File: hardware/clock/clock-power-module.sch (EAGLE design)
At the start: 13 parts, among them U3 L7805, U5 LTC6900IS5PBF

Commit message: main board starting to route
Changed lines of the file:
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@@
 <grid distance="0.1" unitdist="inch" unit="inch" style="lines" multiple="1" display="no" altdistance="0.01" altunitdist="inch" altunit="inch"/>
 <layers>
-<layer number="1" name="Top" color="4" fill="1" visible="yes" active="no"/>
-<layer number="2" name="Route2" color="16" fill="1" visible="yes" active="no"/>
-<layer number="3" name="Route3" color="17" fill="1" visible="yes" active="no"/>
-<layer number="4" name="Route4" color="18" fill="1" visible="yes" active="no"/>
-<layer number="5" name="Route5" color="19" fill="1" visible="yes" active="no"/>
-<layer number="6" name="Route6" color="25" fill="1" visible="yes" active="no"/>
-<layer number="7" name="Route7" color="26" fill="1" visible="yes" active="no"/>
-<layer number="8" name="Route8" color="27" fill="1" visible="yes" active="no"/>
-<layer number="9" name="Route9" color="28" fill="1" visible="yes" active="no"/>
-<layer number="10" name="Route10" color="29" fill="1" visible="yes" active="no"/>
-<layer number="11" name="Route11" color="30" fill="1" visible="yes" active="no"/>
-<layer number="12" name="Route12" color="20" fill="1" visible="yes" active="no"/>
-<layer number="13" name="Route13" color="21" fill="1" visible="yes" active="no"/>
-<layer number="14" name="Route14" color="22" fill="1" visible="yes" active="no"/>
-<layer number="15" name="Route15" color="23" fill="1" visible="yes" active="no"/>
-<layer number="16" name="Bottom" color="1" fill="1" visible="yes" active="no"/>
-<layer number="17" name="Pads" color="2" fill="1" visible="yes" active="no"/>
-<layer number="18" name="Vias" color="2" fill="1" visible="yes" active="no"/>
-<layer number="19" name="Unrouted" color="6" fill="1" visible="yes" active="no"/>
-<layer number="20" name="Dimension" color="24" fill="1" visible="yes" active="no"/>
-<layer number="21" name="tPlace" color="7" fill="1" visible="yes" active="no"/>
-<layer number="22" name="bPlace" color="7" fill="1" visible="yes" active="no"/>
-<layer number="23" name="tOrigins" color="15" fill="1" visible="yes" active="no"/>
-<layer number="24" name="bOrigins" color="15" fill="1" visible="yes" active="no"/>
-<layer number="25" name="tNames" color="7" fill="1" visible="yes" active="no"/>
-<layer number="26" name="bNames" color="7" fill="1" visible="yes" active="no"/>
-<layer number="27" name="tValues" color="7" fill="1" visible="yes" active="no"/>
-<layer number="28" name="bValues" color="7" fill="1" visible="yes" active="no"/>
+<layer number="1" name="Top" color="4" fill="1" visible="no" active="no"/>
+<layer number="2" name="Route2" color="16" fill="1" visible="no" active="no"/>
+<layer number="3" name="Route3" color="17" fill="1" visible="no" active="no"/>
+<layer number="4" name="Route4" color="18" fill="1" visible="no" active="no"/>
+<layer number="5" name="Route5" color="19" fill="1" visible="no" active="no"/>
+<layer number="6" name="Route6" color="25" fill="1" visible="no" active="no"/>
+<layer number="7" name="Route7" color="26" fill="1" visible="no" active="no"/>
+<layer number="8" name="Route8" color="27" fill="1" visible="no" active="no"/>
+<layer number="9" name="Route9" color="28" fill="1" visible="no" active="no"/>
+<layer number="10" name="Route10" color="29" fill="1" visible="no" active="no"/>
+<layer number="11" name="Route11" color="30" fill="1" visible="no" active="no"/>
+<layer number="12" name="Route12" color="20" fill="1" visible="no" active="no"/>
+<layer number="13" name="Route13" color="21" fill="1" visible="no" active="no"/>
+<layer number="14" name="Route14" color="22" fill="1" visible="no" active="no"/>
+<layer number="15" name="Route15" color="23" fill="1" visible="no" active="no"/>
+<layer number="16" name="Bottom" color="1" fill="1" visible="no" active="no"/>
+<layer number="17" name="Pads" color="2" fill="1" visible="no" active="no"/>
+<layer number="18" name="Vias" color="2" fill="1" visible="no" active="no"/>
+<layer number="19" name="Unrouted" color="6" fill="1" visible="no" active="no"/>
+<layer number="20" name="Dimension" color="24" fill="1" visible="no" active="no"/>
+<layer number="21" name="tPlace" color="7" fill="1" visible="no" active="no"/>
+<layer number="22" name="bPlace" color="7" fill="1" visible="no" active="no"/>
+<layer number="23" name="tOrigins" color="15" fill="1" visible="no" active="no"/>
+<layer number="24" name="bOrigins" color="15" fill="1" visible="no" active="no"/>
+<layer number="25" name="tNames" color="7" fill="1" visible="no" active="no"/>
+<layer number="26" name="bNames" color="7" fill="1" visible="no" active="no"/>
+<layer number="27" name="tValues" color="7" fill="1" visible="no" active="no"/>
+<layer number="28" name="bValues" color="7" fill="1" visible="no" active="no"/>
 <layer number="29" name="tStop" color="7" fill="3" visible="no" active="no"/>
 <layer number="30" name="bStop" color="7" fill="6" visible="no" active="no"/>
@@
 <layer number="35" name="tGlue" color="7" fill="4" visible="no" active="no"/>
 <layer number="36" name="bGlue" color="7" fill="5" visible="no" active="no"/>
-<layer number="37" name="tTest" color="7" fill="1" visible="yes" active="no"/>
-<layer number="38" name="bTest" color="7" fill="1" visible="yes" active="no"/>
+<layer number="37" name="tTest" color="7" fill="1" visible="no" active="no"/>
+<layer number="38" name="bTest" color="7" fill="1" visible="no" active="no"/>
 <layer number="39" name="tKeepout" color="4" fill="11" visible="no" active="no"/>
 <layer number="40" name="bKeepout" color="1" fill="11" visible="no" active="no"/>
@@
 <layer number="44" name="Drills" color="7" fill="1" visible="no" active="no"/>
 <layer number="45" name="Holes" color="7" fill="1" visible="no" active="no"/>
-<layer number="46" name="Milling" color="3" fill="1" visible="yes" active="no"/>
-<layer number="47" name="Measures" color="7" fill="1" visible="yes" active="no"/>
-<layer number="48" name="Document" color="7" fill="1" visible="yes" active="no"/>
-<layer number="49" name="Reference" color="7" fill="1" visible="yes" active="no"/>
-<layer number="50" name="dxf" color="7" fill="1" visible="yes" active="no"/>
-<layer number="51" name="tDocu" color="7" fill="1" visible="yes" active="no"/>
-<layer number="52" name="bDocu" color="7" fill="1" visible="yes" active="no"/>
-<layer number="53" name="tGND_GNDA" color="7" fill="9" visible="yes" active="no"/>
-<layer number="54" name="bGND_GNDA" color="1" fill="9" visible="yes" active="no"/>
-<layer number="56" name="wert" color="7" fill="1" visible="yes" active="no"/>
-<layer number="57" name="tCAD" color="7" fill="1" visible="yes" active="no"/>
-<layer number="59" name="tCarbon" color="7" fill="1" visible="yes" active="no"/>
-<layer number="60" name="bCarbon" color="7" fill="1" visible="yes" active="no"/>
+<layer number="46" name="Milling" color="3" fill="1" visible="no" active="no"/>
+<layer number="47" name="Measures" color="7" fill="1" visible="no" active="no"/>
+<layer number="48" name="Document" color="7" fill="1" visible="no" active="no"/>
+<layer number="49" name="Reference" color="7" fill="1" visible="no" active="no"/>
+<layer number="50" name="dxf" color="7" fill="1" visible="no" active="no"/>
+<layer number="51" name="tDocu" color="7" fill="1" visible="no" active="no"/>
+<layer number="52" name="bDocu" color="7" fill="1" visible="no" active="no"/>
+<layer number="53" name="tGND_GNDA" color="7" fill="9" visible="no" active="no"/>
+<layer number="54" name="bGND_GNDA" color="1" fill="9" visible="no" active="no"/>
+<layer number="56" name="wert" color="7" fill="1" visible="no" active="no"/>
+<layer number="57" name="tCAD" color="7" fill="1" visible="no" active="no"/>
+<layer number="59" name="tCarbon" color="7" fill="1" visible="no" active="no"/>
+<layer number="60" name="bCarbon" color="7" fill="1" visible="no" active="no"/>
 <layer number="88" name="SimResults" color="9" fill="1" visible="yes" active="yes"/>
 <layer number="89" name="SimProbes" color="9" fill="1" visible="yes" active="yes"/>
@@
 <junction x="17.78" y="43.18"/>
 <label x="20.32" y="45.72" size="1.778" layer="95"/>
-</segment>
-</net>
+<junction x="27.94" y="43.18"/>
+</segment>
+</net>

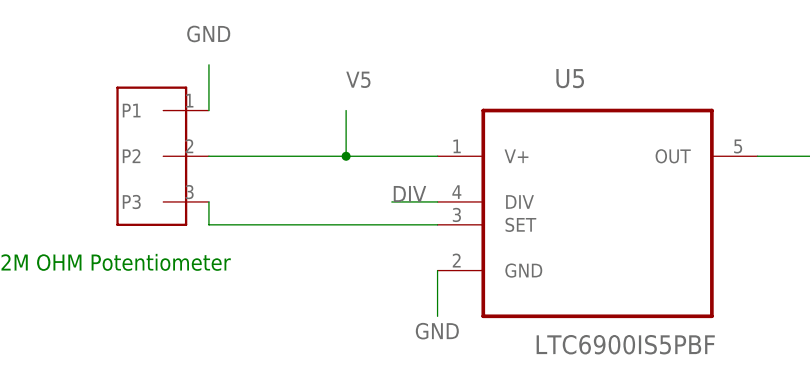
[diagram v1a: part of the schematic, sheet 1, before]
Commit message: update on clock board, so much cleaner now re-layout of main board
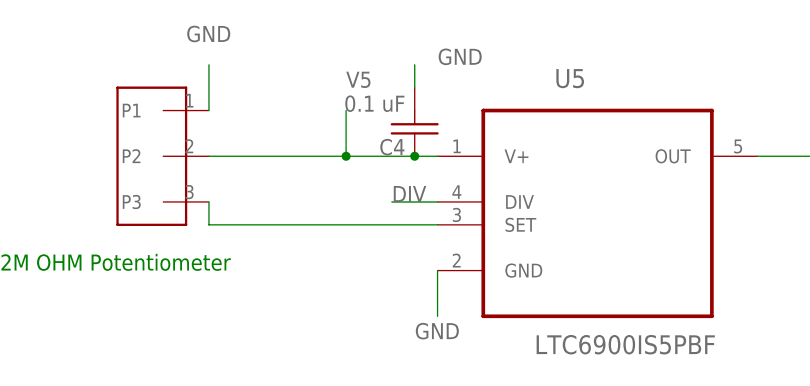
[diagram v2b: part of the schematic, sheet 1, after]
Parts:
- added C4: 0.1 uF, passives:C-USC0805K
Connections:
- net GND: now also C4.2
- net V5: now also C4.1
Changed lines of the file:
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@@
 <part name="C3" library="passives" deviceset="C-US" device="C0805K" package3d_urn="urn:adsk.eagle:package:8089589/1" value="10 uF"/>
 <part name="U$1" library="connector" deviceset="M03" device=""/>
+<part name="C4" library="passives" deviceset="C-US" device="C0805K" package3d_urn="urn:adsk.eagle:package:8089589/1" value="0.1 uF"/>
 </parts>
 <sheets>
@@
 <attribute name="NAME" x="172.72" y="62.738" size="1.778" layer="95" rot="R180"/>
 </instance>
+<instance part="C4" gate="G$1" x="43.18" y="73.66" smashed="yes" rot="R180">
+<attribute name="NAME" x="42.164" y="73.025" size="1.778" layer="95" rot="R180"/>
+<attribute name="VALUE" x="42.164" y="77.851" size="1.778" layer="96" rot="R180"/>
+</instance>
 </instances>
 <busses>
@@
 <label x="162.56" y="60.96" size="1.778" layer="95"/>
 </segment>
+<segment>
+<pinref part="C4" gate="G$1" pin="2"/>
+<wire x1="43.18" y1="78.74" x2="43.18" y2="81.28" width="0.1524" layer="91"/>
+<label x="45.72" y="81.28" size="1.778" layer="95"/>
+</segment>
 </net>
 <net name="V5" class="0">
@@
 <pinref part="U5" gate="A" pin="V+"/>
 <pinref part="U$3" gate="G$1" pin="P2"/>
-<wire x1="45.72" y1="71.12" x2="35.56" y2="71.12" width="0.1524" layer="91"/>
+<wire x1="45.72" y1="71.12" x2="43.18" y2="71.12" width="0.1524" layer="91"/>
+<wire x1="43.18" y1="71.12" x2="35.56" y2="71.12" width="0.1524" layer="91"/>
 <wire x1="35.56" y1="71.12" x2="20.32" y2="71.12" width="0.1524" layer="91"/>
 <wire x1="35.56" y1="71.12" x2="35.56" y2="76.2" width="0.1524" layer="91"/>
 <junction x="35.56" y="71.12"/>
 <label x="35.56" y="78.74" size="1.778" layer="95"/>
+<pinref part="C4" gate="G$1" pin="1"/>
+<junction x="43.18" y="71.12"/>
 </segment>
 <segment>
